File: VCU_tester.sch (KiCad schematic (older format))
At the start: 18 parts, among them J1 Conn_01x08_Male, J2 Screw_Terminal_01x02, J3 USB_B_Micro, J500 Conn_01x08_Female, J501 Conn_01x08_Female, J502 Conn_01x08_Female, J503 Conn_01x08_Female, J504 Conn_01x08_Female, J505 Conn_01x08_Female, J507 Conn_02x18_Odd_Even, P8 BeagleBone_Black_Header, P9 BeagleBone_Black_Header

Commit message: added pin names vcu, rs232 mcguffins, losing hope
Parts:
- removed TP?: TestPoint, symbol Connector:TestPoint
- added TP10, TP11, TP12, TP13, TP14, TP15, TP5, TP6, TP7, TP8, TP9: TestPoint, symbol Connector:TestPoint
- gave numbers to parts that had none: 5
- renumbered J501 to J500, J502 to J501, J504 to J502, J507 to J504, J500 to J505, J503 to J506, J505 to J507
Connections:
- net +5VA is gone; now on net +5V: J500.5 (Pin_5), J500.8 (Pin_8), J504.1 (Pin_1), J504.2 (Pin_2), TP3.1
- net GPIO_10 is gone; now on net GPIO_67: J505.3 (Pin_3)
- net GPIO_11 is gone; now on net GPIO_68: J505.4 (Pin_4)
- net GPIO_4 is gone; now on net GPIO_60: J506.5 (Pin_5)
- net GPIO_5 is gone; now on net GPIO_61: J506.6 (Pin_6)
- net GPIO_6 is gone; now on net GPIO_62: J506.7 (Pin_7)
- net GPIO_69 is gone; now on net GPIO_68: P8.9 (Pin_9)
- net GPIO_7 is gone; now on net GPIO_63: J506.8 (Pin_8)
- net GPIO_8 is gone; now on net GPIO_65: J505.1 (Pin_1)
- net GPIO_9 is gone; now on net GPIO_66: J505.2 (Pin_2)
- net VCURXD3 is gone; now on net UART5_TXD+: J506.1 (Pin_1)
- net VCUTXD3 is gone; now on net UART5_RXD+: J506.2 (Pin_2)
- net +5V: now also D1.1 (A)
- net GNDD: no longer D1.1 (A)
- net GPIO_34: now also D1.3 (RK)
- net GPIO_35: now also D1.4 (GK)
- net GPIO_36: now also D1.2 (BK)
- net GPIO_60: now also TP5.1
- net GPIO_61: now also TP6.1
- net GPIO_62: now also TP7.1
- net GPIO_63: now also TP8.1
- net GPIO_65: now also TP9.1
- net GPIO_66: now also TP10.1
- net GPIO_67: now also J501.1 (Pin_1), TP11.1
- net GPIO_68: now also J505.5 (Pin_5), TP12.1, TP13.1
- net UART5_RXD+: now also TP14.1; no longer J507.6 (Pin_6)
- net UART5_TXD+: now also TP15.1; no longer J507.5 (Pin_5)
- net VCURXD1?: now reaches J506.3 (Pin_3)
- net UART2_RXD renamed BBLR
- net UART2_TXD renamed BBLT
- net UART4_TXD renamed BBRT
- net VCUGPIO_? renamed VCUTXD1?
- net VCURXD1 renamed VCULR
- net VCUTXD1 renamed VCULT
- new net VCURR: J507.5 (Pin_5)
- new net VCURT: J507.6 (Pin_6)
- no-connect marks 78 -> 75
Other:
- note added: "8 GPIOs for user\n(bonus feature !)"
- note added: "ASSTrip"
- note added: "AirCoil1"
- note added: "AirCoil2"
- note added: "AirCoil3"
- note added: "AudioOut"
- note added: "BrakeLights"
- note added: "BrakePSensor2"
- note added: "CAN transcievers"
- note added: "CANEnable"
- note added: "CHECK UARTS. Documentation confusing. CHECK VCU PINS.\nPins do NOT match up with X70 documentation"
- note added: "CONNECT TEMPS/STATES?"
- note added: "CurrSense (!!!!)"
- note added: "J501, J505:\nNOT IN PINOUT UART2\nPIN3 J505, PIN1 J501\nCHECK CHECK CHECK"
- note added: "J506:\nNOT IN PINOUT UART0\nPINS 3/4\nCHECK CHECK CHECK"
- note added: "Motor RS232 Control\nBB VCU"
- note added: "Power / Serial iface (todo?)"
- note added: "PressLout"
- note added: "PressRin"
- note added: "PressRout"
- note added: "TSAL State conn to UART1????\n\nNO SPARE UART FOR BOARD TO BOARD !!!!!"
- note added: "TSALState"
- note added: "TempLin"
- note added: "TempLout\n"
- note added: "TempRin"
- note added: "TempRout\n"
- note added: "UART4 -> UART2"
- note removed: "12 analog pins + 2 dac pins"
- note removed: "8 GPIOs for user"
- note removed: "CAN"
- note removed: "MOTOR CONTROL\nBB VCU"
- note removed: "Power / Serial iface (todo)"
- note removed: "TO ROUTE:\n8 GPIOs (only have four - I2C?), UARTMC1, UARTMC2"
- note removed: "TODO:\nGet CAN TX and RX for BOTH BB and VCU"
- note removed: "UART3 -> UART2"
- note removed: "check how to power - 5V0? appears to o/p of vcu brd reg"
- note removed: "need two UARTs for Motors?"
- moved on the sheet: D1, J2, J3

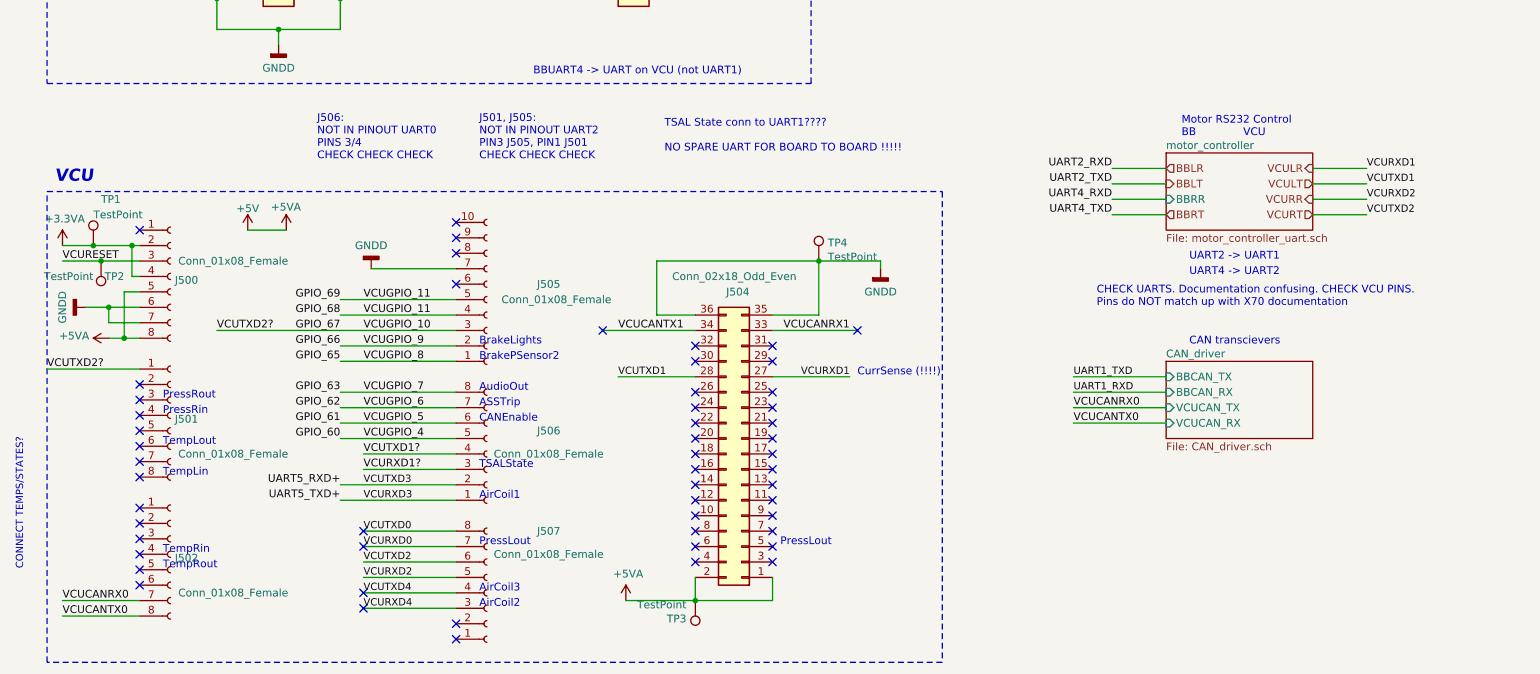
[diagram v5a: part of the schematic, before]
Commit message: misread diagram.. fixed
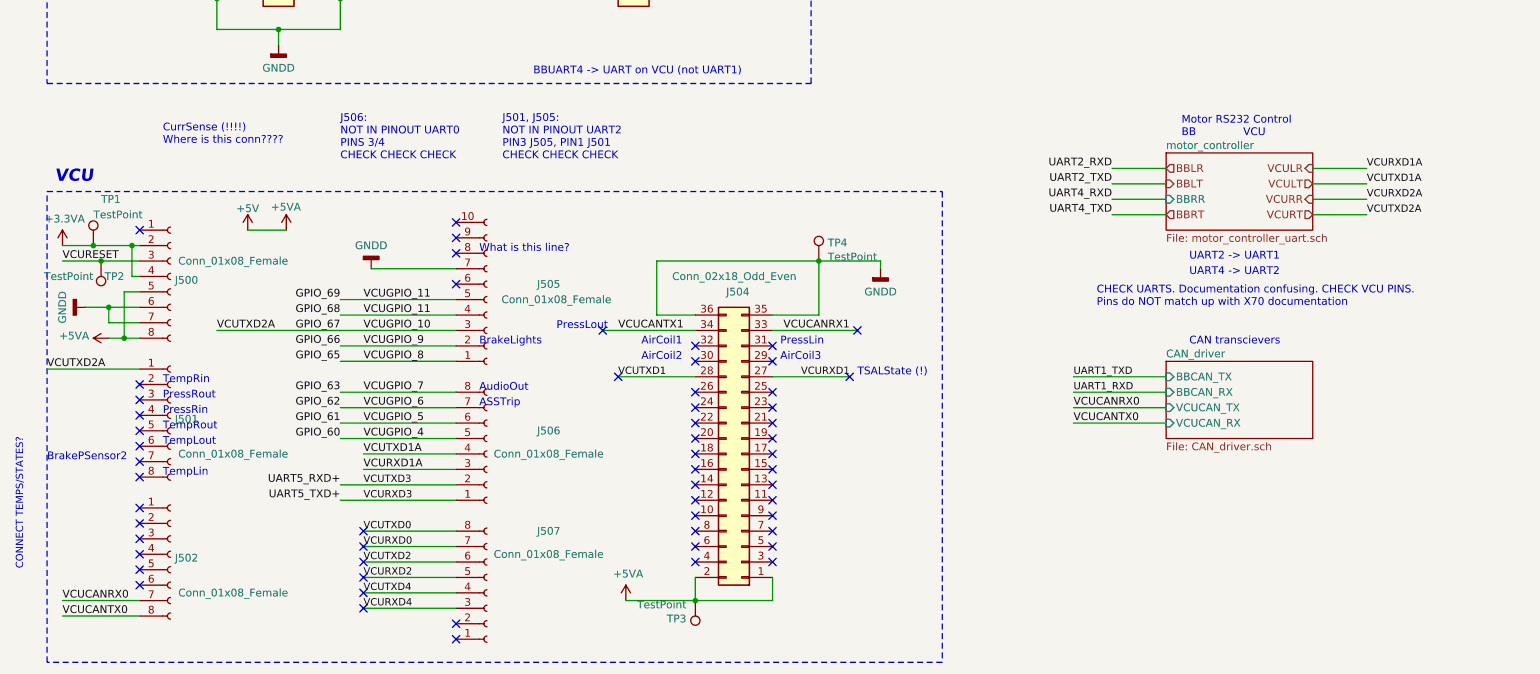
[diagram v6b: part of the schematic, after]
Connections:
- net GPIO_67 is gone; now on net VCURT: J501.1 (Pin_1), J505.3 (Pin_3), P8.8 (Pin_8), TP11.1
- net VCURXD1? is gone; now on net VCULR: J506.3 (Pin_3)
- net VCUTXD1? is gone; now on net VCULT: J506.4 (Pin_4)
- net VCULR: no longer J504.27 (Pin_27)
- net VCULT: no longer J504.28 (Pin_28)
- net VCURR: no longer J507.5 (Pin_5)
- net VCURT: no longer J507.6 (Pin_6)
- new net VCURXD1: J504.27 (Pin_27)
- new net VCURXD2: J507.5 (Pin_5)
- new net VCUTXD1: J504.28 (Pin_28)
- new net VCUTXD2: J507.6 (Pin_6)
- no-connect marks 75 -> 79
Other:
- note added: "CurrSense (!!!!)\nWhere is this conn????"
- note added: "PressLin"
- note added: "TSALState (!)"
- note added: "What is this line?"
- note removed: "CANEnable"
- note removed: "CurrSense (!!!!)"
- note removed: "TSAL State conn to UART1????\n\nNO SPARE UART FOR BOARD TO BOARD !!!!!"
- note removed: "TSALState"
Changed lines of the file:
@@
 NoConn ~ 5150 6200
 Text Label 9500 4750 0    47   ~ 0
-VCUTXD2
+VCUTXD2A
 Text Label 9500 4650 0    47   ~ 0
-VCURXD2
+VCURXD2A
 NoConn ~ 6200 5500
 NoConn ~ 4550 5500
@@
 BBRT
 Text Label 9500 4550 0    47   ~ 0
-VCUTXD1
+VCUTXD1A
 Text Label 9500 4450 0    47   ~ 0
-VCURXD1
+VCURXD1A
 Wire Wire Line
 	2850 6500 3600 6500
@@
 	0    -1   -1   0
 $EndComp
-Text Notes 3750 5700 0    50   ~ 0
-BrakePSensor2
-Text Notes 1700 7050 0    50   ~ 0
+Text Notes 1700 6150 0    50   ~ 0
 TempRout\n
-Text Notes 1700 6950 0    50   ~ 0
+Text Notes 1700 5850 0    50   ~ 0
 TempRin
 Text Notes 1700 6450 0    50   ~ 0
@@
 Text Notes 1700 6050 0    50   ~ 0
 PressRin
-Text Notes 6200 5800 0    50   ~ 0
-CurrSense (!!!!)
-Text Notes 5700 6900 0    50   ~ 0
-PressLout
-Text Notes 3750 6900 0    50   ~ 0
+Text Notes 1700 4300 0    50   ~ 0
+CurrSense (!!!!)\nWhere is this conn????
+Text Notes 5700 5600 0    50   ~ 0
+PressLin
+Text Notes 4250 5500 0    50   ~ 0
 PressLout
 Wire Wire Line
 	3600 6300 3000 6300
 Text Label 3000 6300 0    50   ~ 0
-VCUTXD1?
+VCUTXD1A
 Wire Wire Line
 	3000 6400 3600 6400
 Text Label 3000 6400 0    50   ~ 0
-VCURXD1?
-Text Notes 2700 4400 0    50   ~ 0
+VCURXD1A
+Text Notes 2850 4400 0    50   ~ 0
 J506:\nNOT IN PINOUT UART0\nPINS 3/4\nCHECK CHECK CHECK
 Wire Wire Line
 	1550 5750 950  5750
 Text Label 950  5750 0    50   ~ 0
-VCUTXD2?
+VCUTXD2A
 Text Label 2050 5500 0    50   ~ 0
-VCUTXD2?
+VCUTXD2A
 Wire Wire Line
 	2050 5500 3600 5500
-Text Notes 3750 4400 0    50   ~ 0
+Text Notes 3900 4400 0    50   ~ 0
 J501, J505:\nNOT IN PINOUT UART2\nPIN3 J505, PIN1 J501\nCHECK CHECK CHECK
 Wire Wire Line
 	2850 6000 3600 6000
-Text Notes 3750 6100 0    50   ~ 0
-CANEnable
 $Comp
 L power:+5V #PWR0116
@@
 Text Notes 3750 6000 0    50   ~ 0
 ASSTrip
-Text Notes 3750 6400 0    50   ~ 0
-TSALState
-Text Notes 4950 4350 0    50   ~ 0
-TSAL State conn to UART1????\n\nNO SPARE UART FOR BOARD TO BOARD !!!!!
-Text Notes 3750 7300 0    50   ~ 0
+Text Notes 6200 5800 0    50   ~ 0
+TSALState (!)
+Text Notes 4800 5700 0    50   ~ 0
 AirCoil2
-Text Notes 3750 6600 0    50   ~ 0
+Text Notes 4800 5600 0    50   ~ 0
 AirCoil1
-Text Notes 3750 7200 0    50   ~ 0
+Text Notes 5700 5700 0    50   ~ 0
 AirCoil3
+Text Notes 3750 5000 0    50   ~ 0
+What is this line?
+NoConn ~ 3000 7100
+NoConn ~ 3000 7000
+Text Notes 950  6350 0    50   ~ 0
+BrakePSensor2
+NoConn ~ 4650 5800
+NoConn ~ 6150 5800
 $EndSCHEMATC

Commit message: sleep isn't real. Fixed pins. DAC hell. Nearly done on schematic.
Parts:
- removed J3: USB_B_Micro, symbol Connector:USB_B_Micro
- removed TP10: TestPoint, symbol Connector:TestPoint
- added C?: 100p, symbol Device:C
- added C?: 10u, symbol Device:C
- added P?: USB_C_Plug_USB2.0, symbol Connector:USB_C_Plug_USB2.0
- added TP? (x19): TestPoint, symbol Connector:TestPoint
- added U?: REF3020, Package_TO_SOT_SMD:SOT-23, symbol Reference_Voltage:REF3020
- added U?: TLV5631IDW, DW0020A_N, symbol TLV5631IDW:TLV5631IDW
- J1: value Conn_01x08_Male -> Conn_01x04_Male; symbol Connector:Conn_01x08_Male -> Connector:Conn_01x04_Male
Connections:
- net ETHRPWM1A is gone; now on net GPIO_50: P9.14 (Pin_14)
- net ETHRPWM1B is gone; now on net GPIO_51: P9.16 (Pin_16)
- net VCURXD1 is gone; now on net GPIO_22: J504.27 (Pin_27)
- net +5V: now also J2.2 (Pin_2), P?.A4 (VBUS), P?.A9 (VBUS), P?.B4 (VBUS), P?.B9 (VBUS), U?.1 (IN), U?.11 (AVDD), U?.20 (DVDD)
- net GNDD: now also C?.2, C?.2, P?.A1 (GND), P?.A12 (GND), P?.B1 (GND), P?.B12 (GND), U?.1 (DGND), U?.10 (AGND), U?.3 (GND)
- net GPIO_115: now also D1.4 (GK)
- net GPIO_117: now also D1.3 (RK)
- net GPIO_36: no longer D1.2 (BK)
- net GPIO_44: now also J504.3 (Pin_3), TP?.1
- net GPIO_45: now also J504.4 (Pin_4), TP?.1
- net GPIO_46: now also J504.5 (Pin_5), TP?.1
- net GPIO_47: now also J504.6 (Pin_6), TP?.1
- net GPIO_48: now also J504.7 (Pin_7), TP?.1
- net GPIO_49: now also J504.8 (Pin_8), TP?.1
- net GPIO_60: now also J1.1 (Pin_1); no longer J506.5 (Pin_5)
- net GPIO_61: now also J1.2 (Pin_2); no longer J506.6 (Pin_6)
- net GPIO_62: no longer J506.7 (Pin_7), TP7.1
- net GPIO_63: no longer J506.8 (Pin_8), TP8.1
- net GPIO_65: now also J1.3 (Pin_3), TP7.1; no longer J505.1 (Pin_1), TP9.1
- net GPIO_66: now also J1.4 (Pin_4), TP8.1; no longer J505.2 (Pin_2)
- net GPIO_68: now also J2.1 (Pin_1); no longer J505.4 (Pin_4), J505.5 (Pin_5), P8.9 (Pin_9), TP12.1, TP13.1
- net GPIO_70: no longer J1.1 (Pin_1)
- net GPIO_71: no longer J1.2 (Pin_2)
- net GPIO_72: no longer J1.3 (Pin_3)
- net GPIO_73: no longer J1.4 (Pin_4)
- net GPIO_74: no longer J1.5 (Pin_5)
- net GPIO_75: no longer J1.6 (Pin_6)
- net GPIO_76: no longer J1.7 (Pin_7)
- net GPIO_77: no longer J1.8 (Pin_8)
- net UART1_RXD: now also J506.2 (Pin_2), TP?.1
- net UART1_TXD: now also J506.1 (Pin_1), TP?.1
- net UART5_RXD+: no longer J506.2 (Pin_2), TP14.1
- net UART5_TXD+: no longer J506.1 (Pin_1), TP15.1
- net VCURT: no longer P8.8 (Pin_8), TP11.1
- net TempRin: now reaches J501.2 (Pin_2)
- net TempRin: now also TP15.1, U?.14 (OUTC)
- net PressRout: now reaches J501.3 (Pin_3)
- net PressRout: now also TP14.1, U?.9 (OUTH)
- net PressRin: now reaches J501.4 (Pin_4)
- net PressRin: now also TP13.1, U?.8 (OUTG)
- net TempRout: now reaches J501.5 (Pin_5)
- net TempRout: now also TP12.1, U?.15 (OUTD)
- net TempLout: now reaches J501.6 (Pin_6)
- net TempLout: now also TP11.1, U?.13 (OUTB)
- net TempLin: now reaches J501.8 (Pin_8)
- net TempLin: now also TP9.1, U?.12 (OUTA)
- net GPIO_51: now reaches J504.10 (Pin_10)
- net GPIO_51: now also TP?.1
- net AIR3: now reaches J504.29 (Pin_29)
- net AIR3: now also TP?.1
- net AIR2: now reaches J504.30 (Pin_30)
- net AIR2: now also TP?.1
- net PressLin: now reaches J504.31 (Pin_31)
- net PressLin: now also TP?.1, U?.6 (OUTE)
- net AIR1: now reaches J504.32 (Pin_32)
- net AIR1: now also TP?.1
- net GPIO_50: now reaches J504.9 (Pin_9)
- net GPIO_50: now also TP?.1
- net VCU_REFVOLT: now reaches J505.8 (Pin_8)
- net VCU_REFVOLT: now also C?.1, C?.1, U?.16 (REF), U?.2 (OUT)
- net ETHRPWM2A renamed GPIO_22
- net GPIO_22: now also TP?.1
- net ETHRPWM2B renamed GPIO_23
- net GPIO_34 renamed MMC1_Dat2
- net MMC1_Dat2: no longer D1.3 (RK)
- net GPIO_35 renamed MMC1_dat3
- net MMC1_dat3: no longer D1.4 (GK)
- net GPIO_38 renamed MMC1_Dat6
- net MMC1_Dat6: no longer J2.1 (Pin_1)
- net GPIO_39 renamed MMC1_dat7
- net MMC1_dat7: no longer J2.2 (Pin_2)
- net SP11_CSO renamed SPI1_CSO
- net SP11_DO renamed SPI1_DO
- net SPI1_DO: now also U?.2 (DIN)
- net SP11_SCLK renamed SPI1_SCLK
- net SPI1_SCLK: now also U?.3 (SCLK)
- net SPIO_CSO renamed DCAN0_RX
- net SPIO_D1 renamed DCAN0_TX
- net VCUCANTX1 renamed PressLout
- net PressLout: now also TP?.1, U?.7 (OUTF)
- new net GPIO_4: J505.2 (Pin_2), TP?.1
- new net GPIO_5: J506.8 (Pin_8), TP?.1
- new net GPIO_67: P8.8 (Pin_8)
- new net GPIO_69: D1.2 (BK), P8.9 (Pin_9)
- new net GPIO_7: J506.7 (Pin_7), TP?.1
- new net VCUGPIO_11: J505.4 (Pin_4), J505.5 (Pin_5)
- new net VCUGPIO_4: J506.5 (Pin_5)
- new net VCUGPIO_5: J506.6 (Pin_6)
- new net VCUGPIO_8: J505.1 (Pin_1)
- no-connect marks 79 -> 84
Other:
- note added: "4 GPIOs for user\n(bonus feature !)"
- note added: "CHECK UARTS. Documentation confusing. CHECK VCU PINS.\nPins do NOT match up with X70 documentation for UARTS"
- note added: "CHECK!!\nCSO may not be appropriate.\nTiming may need to be modified.\n\nDatasheet is a mess.\nNo SPI support but it says it does??"
- note added: "External Probe (Future use)"
- note added: "Non RS232/CAN Testpoints"
- note added: "VCU Reference Voltage\n2.048V"
- note added: "VCU SPI DAC 8ch"
- note added: "tsal state"
- note removed: "8 GPIOs for user\n(bonus feature !)"
- note removed: "AirCoil1"
- note removed: "AirCoil2"
- note removed: "AirCoil3"
- note removed: "BrakePSensor2"
- note removed: "CHECK UARTS. Documentation confusing. CHECK VCU PINS.\nPins do NOT match up with X70 documentation"
- note removed: "CONNECT TEMPS/STATES?"
- note removed: "PressLin"
- note removed: "PressLout"
- note removed: "PressRin"
- note removed: "PressRout"
- note removed: "Shutdown Circuit Status Observer"
- note removed: "TSALState (!)"
- note removed: "TempLin"
- note removed: "TempLout\n"
- note removed: "TempRin"
- note removed: "TempRout\n"
- note removed: "What is this line?"
- note removed: "gpio 22"
- note removed: "gpio 23"
- moved on the sheet: D1, J2, J500, J501, J502, J504, J505, J506, J507, P8, P9, TP1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
